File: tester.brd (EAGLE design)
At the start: 56 x 67 mm, 72 parts, among them IC1 ATmega8/88/168, K1 NA 05W K, M1 SP6000C-180, P1 250, P2 10k lin, Q1 BC847CSMD, Q2 BC847CSMD, Q3 BC807-40SMD, Q4 8,000 MHz, Q5 BC847CSMD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

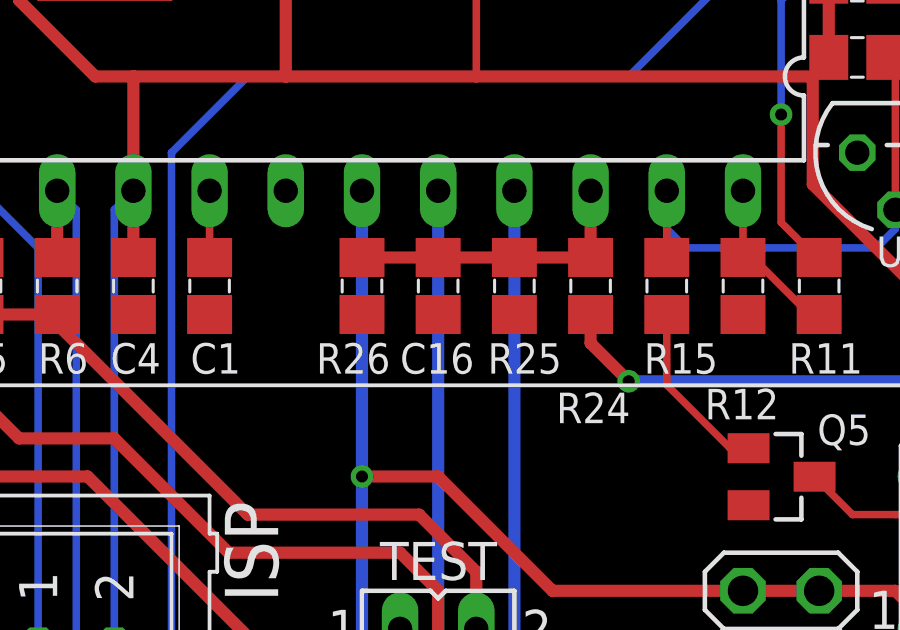
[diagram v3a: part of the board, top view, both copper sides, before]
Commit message: Revert "fix for reichelt"
This reverts commit 00bdf40ca26db270fa33158348546dbcbdb5b146.

Reichelt offers 162K/18K => 1:10-divider
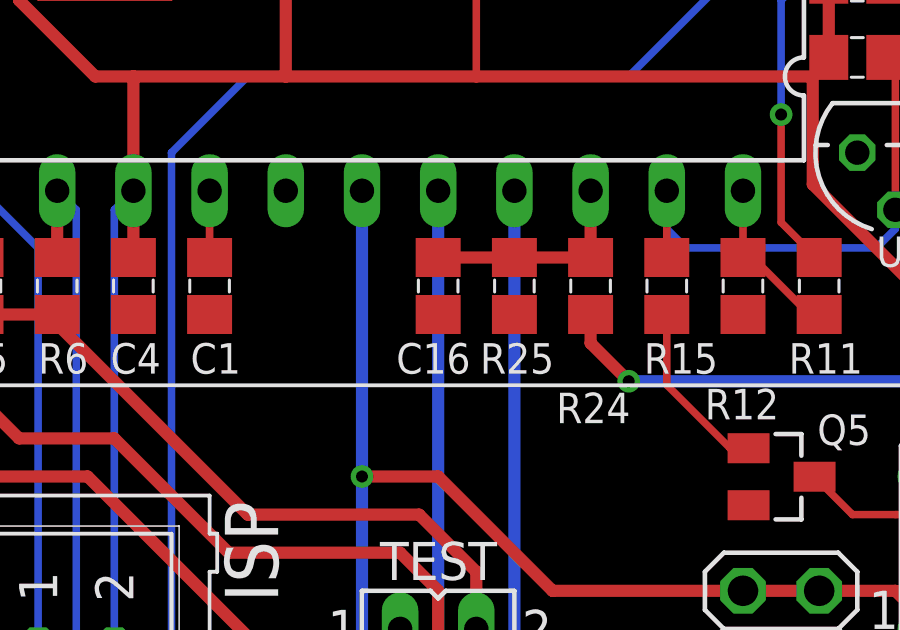
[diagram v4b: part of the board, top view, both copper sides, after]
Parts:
- removed R26: inf, resistor:R0805
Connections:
- net GND: no longer R26.1
- net PC3: no longer R26.2
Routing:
- net PC3: track 10.2 -> 7.45 mm
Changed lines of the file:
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@@
 <variantdefs>
 <variantdef name="nopwm"/>
-<variantdef name="no20k"/>
 </variantdefs>
 <classes>
@@
 <element name="R25" library="resistor" package="R0805" value="20k" x="30.48" y="25.4" smashed="yes" rot="R90">
 <attribute name="TOLERANCE" value="0.1%" x="30.48" y="25.4" size="1.778" layer="27" rot="R90" display="off"/>
-<attribute name="NAME" x="29.591" y="22.479" size="1.016" layer="25"/>
+<attribute name="NAME" x="29.337" y="22.479" size="1.016" layer="25"/>
 <attribute name="VALUE" x="32.512" y="24.511" size="1.27" layer="27" rot="R90"/>
-<variant name="no20k" value="22k"/>
 </element>
 <element name="C16" library="rcl" package="C0805" value="10n" x="27.94" y="25.4" smashed="yes" rot="R270">
-<attribute name="NAME" x="26.67" y="22.479" size="1.016" layer="25"/>
+<attribute name="NAME" x="26.543" y="22.479" size="1.016" layer="25"/>
 <attribute name="VALUE" x="26.035" y="26.035" size="1.27" layer="27" rot="R270"/>
 </element>
@@
 <element name="JP7" library="con-lsta" package="FE02-1" value="TEST2" x="27.94" y="13.97" smashed="yes">
 <attribute name="VALUE" x="25.4" y="11.176" size="1.27" layer="27" ratio="10"/>
-</element>
-<element name="R26" library="resistor" package="R0805" value="inf" x="25.4" y="25.4" smashed="yes" rot="R90">
-<attribute name="TOLERANCE" value="0.1%" x="25.4" y="25.4" size="1.778" layer="27" rot="R90" display="off"/>
-<attribute name="NAME" x="23.876" y="22.479" size="1.016" layer="25"/>
-<attribute name="VALUE" x="27.94" y="24.13" size="1.27" layer="27" rot="R90"/>
-<variant name="no20k" value="220k"/>
 </element>
 </elements>
@@
 <contactref element="Q5" pad="2"/>
 <contactref element="P2" pad="E"/>
-<contactref element="R26" pad="1"/>
 </signal>
 <signal name="N$5">
@@
 <wire x1="28.04" y1="26.25" x2="27.94" y2="26.35" width="0.4064" layer="1"/>
 <wire x1="30.48" y1="26.35" x2="27.94" y2="26.35" width="0.4064" layer="1"/>
-<contactref element="R26" pad="2"/>
-<wire x1="28.04" y1="26.25" x2="28.04" y2="26.35" width="0.4064" layer="1"/>
-<wire x1="28.04" y1="26.35" x2="25.4" y2="26.35" width="0.4064" layer="1"/>
 </signal>
 <signal name="N$24">

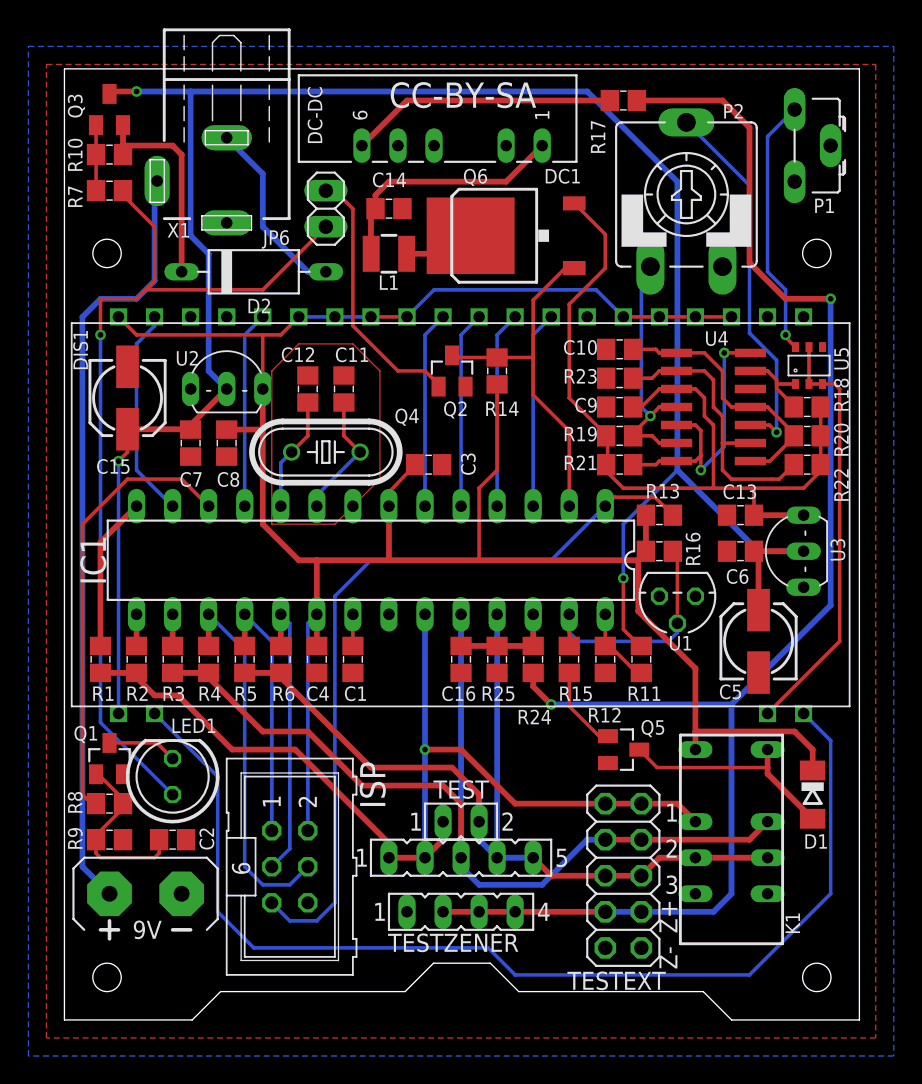
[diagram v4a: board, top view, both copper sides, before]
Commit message: corrected angles
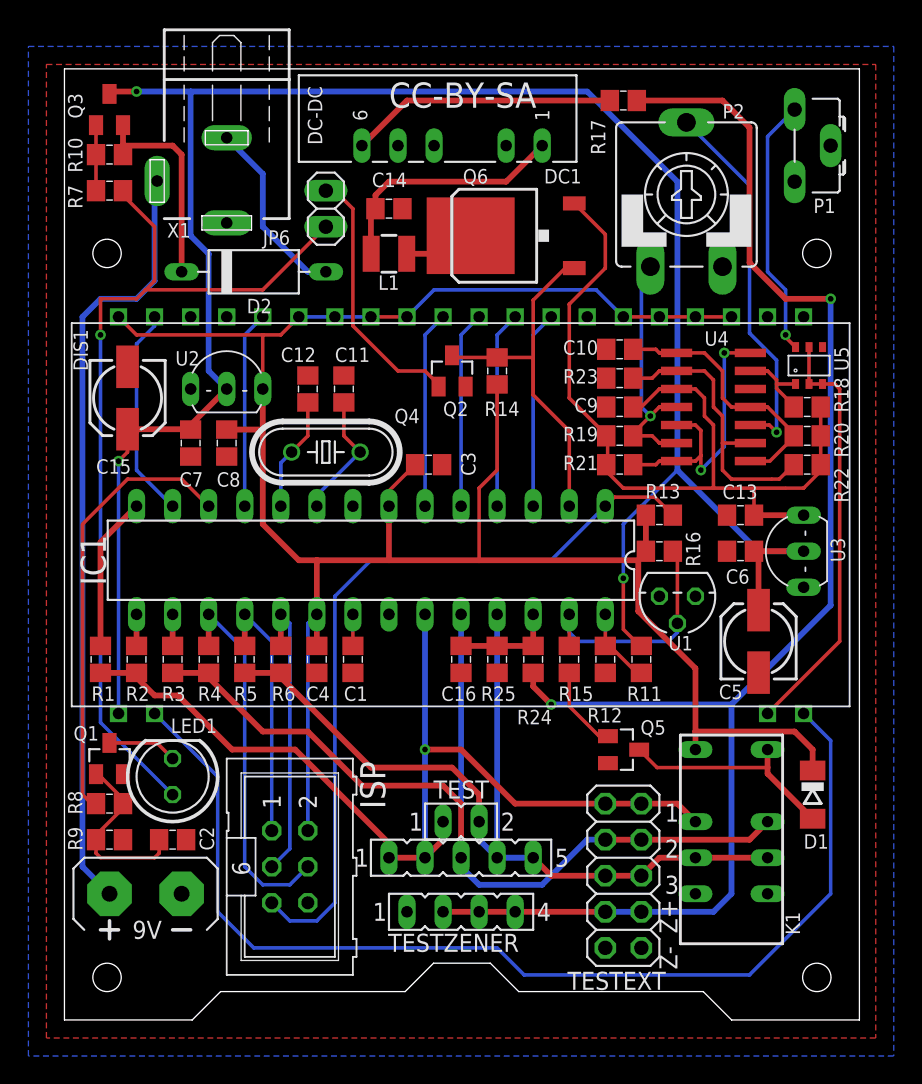
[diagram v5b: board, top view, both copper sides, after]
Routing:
- net N$14: track 34.8 -> 0.00 mm
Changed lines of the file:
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@@
 <rectangle x1="51.07" y1="45.2" x2="52.17" y2="45.3" layer="41"/>
 <rectangle x1="52.67" y1="45.2" x2="53.87" y2="45.3" layer="41"/>
+<wire x1="16.51" y1="47.625" x2="20.32" y2="47.625" width="0.254" layer="41"/>
+<wire x1="20.32" y1="47.625" x2="22.225" y2="45.72" width="0.254" layer="41"/>
+<wire x1="22.225" y1="45.72" x2="22.225" y2="38.1" width="0.254" layer="41"/>
+<wire x1="22.225" y1="38.1" x2="20.955" y2="36.83" width="0.254" layer="41"/>
+<wire x1="19.685" y1="35.56" x2="19.05" y2="34.925" width="0.254" layer="41"/>
+<wire x1="19.05" y1="34.925" x2="14.605" y2="34.925" width="0.254" layer="41"/>
+<wire x1="14.605" y1="34.925" x2="14.605" y2="45.72" width="0.254" layer="41"/>
+<wire x1="14.605" y1="45.72" x2="16.51" y2="47.625" width="0.254" layer="41"/>
 </plain>
 <attributes>
@@
 <wire x1="29.21" y1="37.465" x2="29.21" y2="32.385" width="0.254" layer="1"/>
 <wire x1="22.86" y1="36.195" x2="22.86" y2="37.172" width="0.254" layer="1"/>
-<wire x1="22.86" y1="37.172" x2="24.704" y2="39.116" width="0.254" layer="1"/>
 <wire x1="29.21" y1="32.385" x2="40.425" y2="32.385" width="0.4064" layer="1"/>
 <wire x1="13.97" y1="34.925" x2="13.97" y2="41.59" width="0.4064" layer="1"/>
@@
 <wire x1="40.425" y1="32.385" x2="40.425" y2="32.485" width="0.25" layer="1"/>
 <wire x1="40.425" y1="32.485" x2="40.96" y2="33.02" width="0.25" layer="1"/>
+<wire x1="22.86" y1="37.172" x2="22.86" y2="37.272" width="0.25" layer="1"/>
+<wire x1="22.86" y1="37.272" x2="24.704" y2="39.116" width="0.25" layer="1"/>
 </signal>
 <signal name="PC0">
@@
 <contactref element="DC1" pad="1"/>
 <contactref element="L1" pad="2"/>
-<wire x1="21.61" y1="53.975" x2="21.59" y2="54.095" width="0.4064" layer="1"/>
 <wire x1="21.59" y1="54.095" x2="21.59" y2="57.15" width="0.4064" layer="1"/>
 <wire x1="21.59" y1="57.15" x2="21.91" y2="57.15" width="0.4064" layer="1"/>
@@
 <wire x1="22.86" y1="59.055" x2="31.115" y2="59.055" width="0.4064" layer="1"/>
 <wire x1="31.115" y1="59.055" x2="33.655" y2="61.595" width="0.4064" layer="1"/>
+<wire x1="21.61" y1="53.975" x2="21.59" y2="53.995" width="0.25" layer="1"/>
+<wire x1="21.59" y1="53.995" x2="21.59" y2="54.095" width="0.25" layer="1"/>
 </signal>
 <signal name="N$28">
@@
 <wire x1="10.795" y1="17.145" x2="10.795" y2="7.62" width="0.254" layer="16"/>
 <wire x1="10.795" y1="7.62" x2="13.335" y2="5.08" width="0.254" layer="16"/>
-<wire x1="13.335" y1="5.08" x2="29.845" y2="5.08" width="0.254" layer="16"/>
-<wire x1="29.845" y1="5.08" x2="31.75" y2="3.175" width="0.254" layer="16"/>
-<wire x1="31.75" y1="3.175" x2="48.26" y2="3.175" width="0.254" layer="16"/>
+<wire x1="13.335" y1="5.08" x2="30.48" y2="5.08" width="0.254" layer="16"/>
+<wire x1="30.48" y1="5.08" x2="32.385" y2="3.175" width="0.254" layer="16"/>
+<wire x1="32.385" y1="3.175" x2="48.26" y2="3.175" width="0.254" layer="16"/>
 <wire x1="48.26" y1="3.175" x2="53.975" y2="8.89" width="0.254" layer="16"/>
 <wire x1="53.975" y1="8.89" x2="53.975" y2="19.685" width="0.254" layer="16"/>
@@
 <wire x1="41.749" y1="17.78" x2="40.486" y2="19.043" width="0.25" layer="1"/>
 </signal>
-<signal name="N$14">
-<wire x1="19.685" y1="35.56" x2="19.05" y2="34.925" width="0" layer="1"/>
-<wire x1="19.05" y1="34.925" x2="14.605" y2="34.925" width="0" layer="1"/>
-<wire x1="14.605" y1="34.925" x2="14.605" y2="45.72" width="0" layer="1"/>
-<wire x1="14.605" y1="45.72" x2="16.51" y2="47.625" width="0" layer="1"/>
-<wire x1="16.51" y1="47.625" x2="20.32" y2="47.625" width="0" layer="1"/>
-<wire x1="20.32" y1="47.625" x2="22.225" y2="45.72" width="0" layer="1"/>
-<wire x1="22.225" y1="45.72" x2="22.225" y2="38.1" width="0" layer="1"/>
-<wire x1="22.225" y1="38.1" x2="20.955" y2="36.83" width="0" layer="1"/>
-</signal>
 </signals>
+<errors>
+</errors>
 </board>
 </drawing>

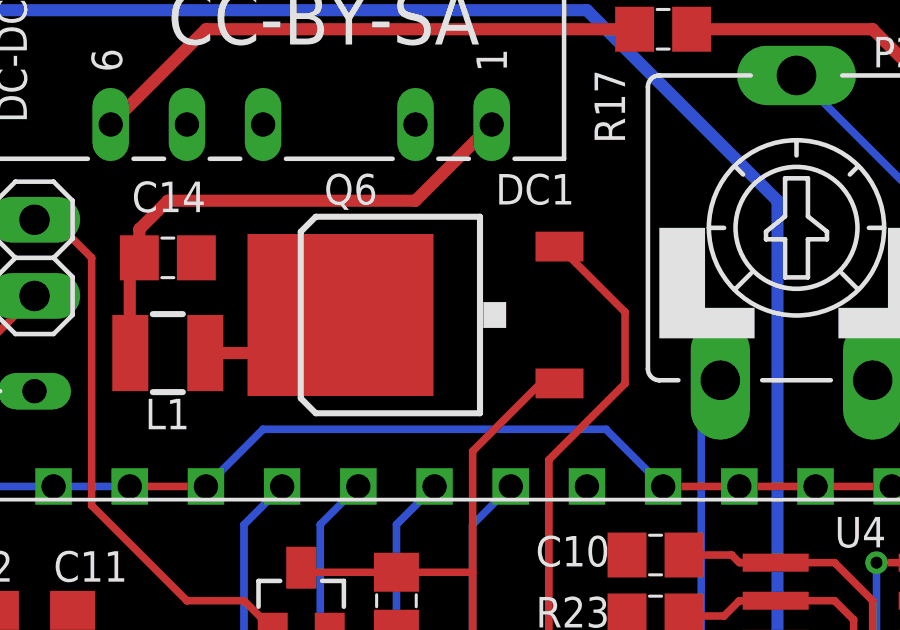
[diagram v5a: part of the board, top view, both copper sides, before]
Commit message: IRLML 6402 for Q6
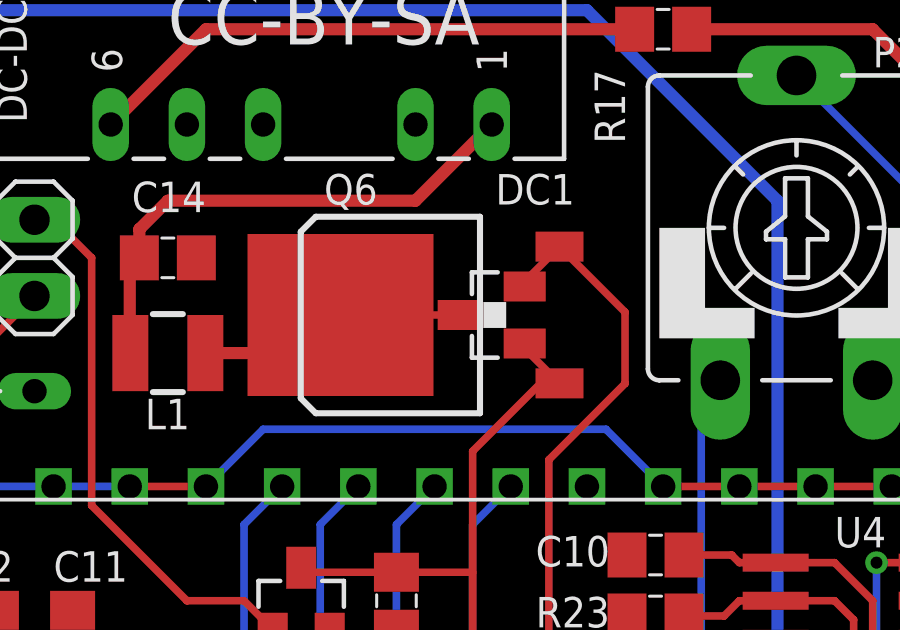
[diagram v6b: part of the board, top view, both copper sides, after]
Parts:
- added Q6/B: IRLML6402, mosfet:MICRO3
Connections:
- net +5V/2: now also Q6/B.2
- net N$24: now also Q6/B.3
- net PD0: now also Q6/B.1
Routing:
- net N$24: track 5.03 -> 8.97 mm
- net +5V/2: track 60.6 -> 62.4 mm
- net PD0: track 28.3 -> 30.1 mm
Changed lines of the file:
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@@
 <attribute name="VALUE" x="25.4" y="11.176" size="1.27" layer="27" ratio="10"/>
+</element>
+<element name="Q6/B" library="mosfet" package="MICRO3" value="IRLML6402" x="33.655" y="55.245" smashed="yes" rot="R90">
+<attribute name="VALUE" x="36.83" y="53.34" size="1.27" layer="27" rot="R90"/>
 </element>
 </elements>
@@
 <wire x1="28.615" y1="55.245" x2="27.345" y2="53.975" width="0.4064" layer="1"/>
 <wire x1="27.345" y1="53.975" x2="24.11" y2="53.975" width="0.4064" layer="1"/>
+<contactref element="Q6/B" pad="3"/>
+<wire x1="28.615" y1="55.245" x2="32.555" y2="55.245" width="0.25" layer="1"/>
 </signal>
 <signal name="N$25">
@@
 <wire x1="38.266" y1="38.569" x2="38.266" y2="39.016" width="0.25" layer="1"/>
 <wire x1="38.266" y1="39.016" x2="38.166" y2="39.116" width="0.25" layer="1"/>
+<contactref element="Q6/B" pad="2"/>
+<wire x1="34.755" y1="56.195" x2="34.755" y2="56.365" width="0.25" layer="1"/>
+<wire x1="34.755" y1="56.365" x2="35.915" y2="57.525" width="0.25" layer="1"/>
 </signal>
 <signal name="V+">
@@
 <wire x1="30.48" y1="46.67" x2="27.305" y2="46.67" width="0.25" layer="1"/>
 <wire x1="27.305" y1="46.67" x2="27.305" y2="46.82" width="0.25" layer="1"/>
+<contactref element="Q6/B" pad="1"/>
+<wire x1="34.755" y1="54.295" x2="34.755" y2="54.125" width="0.25" layer="1"/>
+<wire x1="34.755" y1="54.125" x2="35.915" y2="52.965" width="0.25" layer="1"/>
 </signal>
 <signal name="PD4">
@@
 </signal>
 </signals>
-<errors>
-</errors>
 </board>
 </drawing>

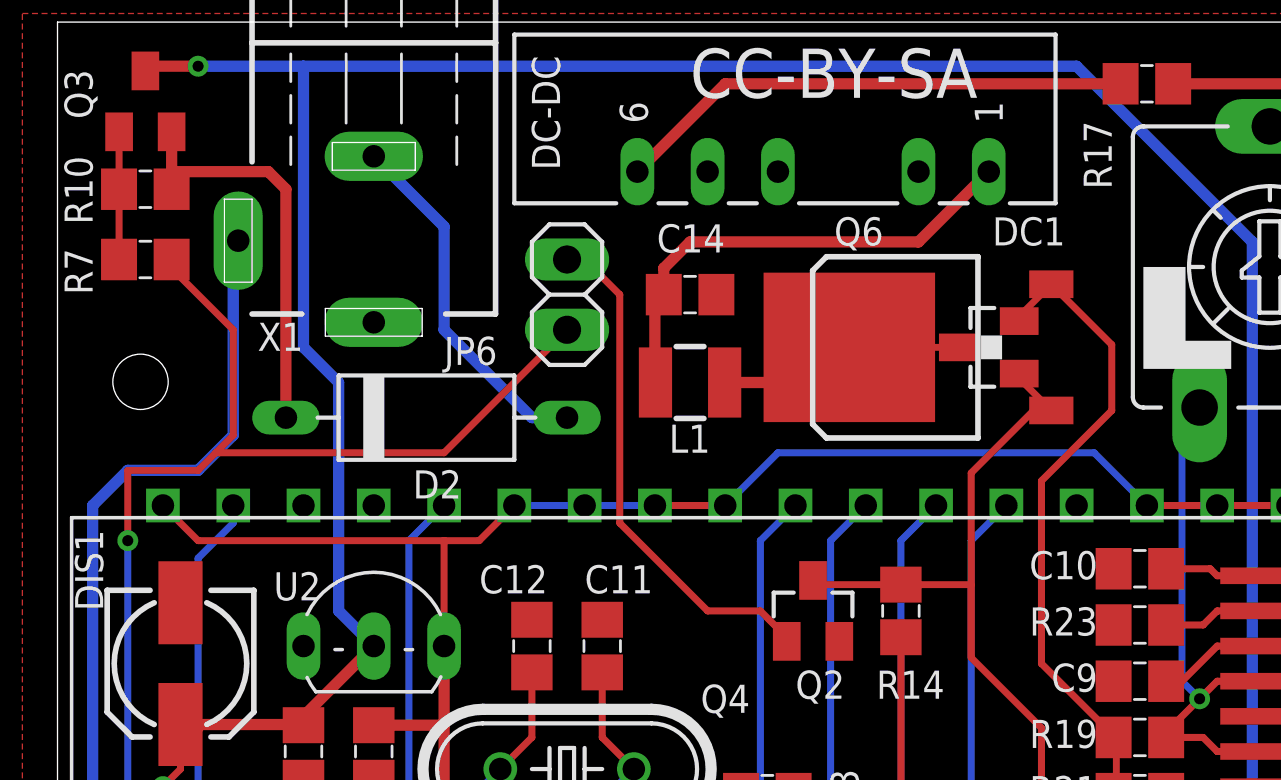
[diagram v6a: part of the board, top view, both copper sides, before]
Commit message: change q6, s1
remove q6 option for irfr9024
tactile switch s1 instead of pin header
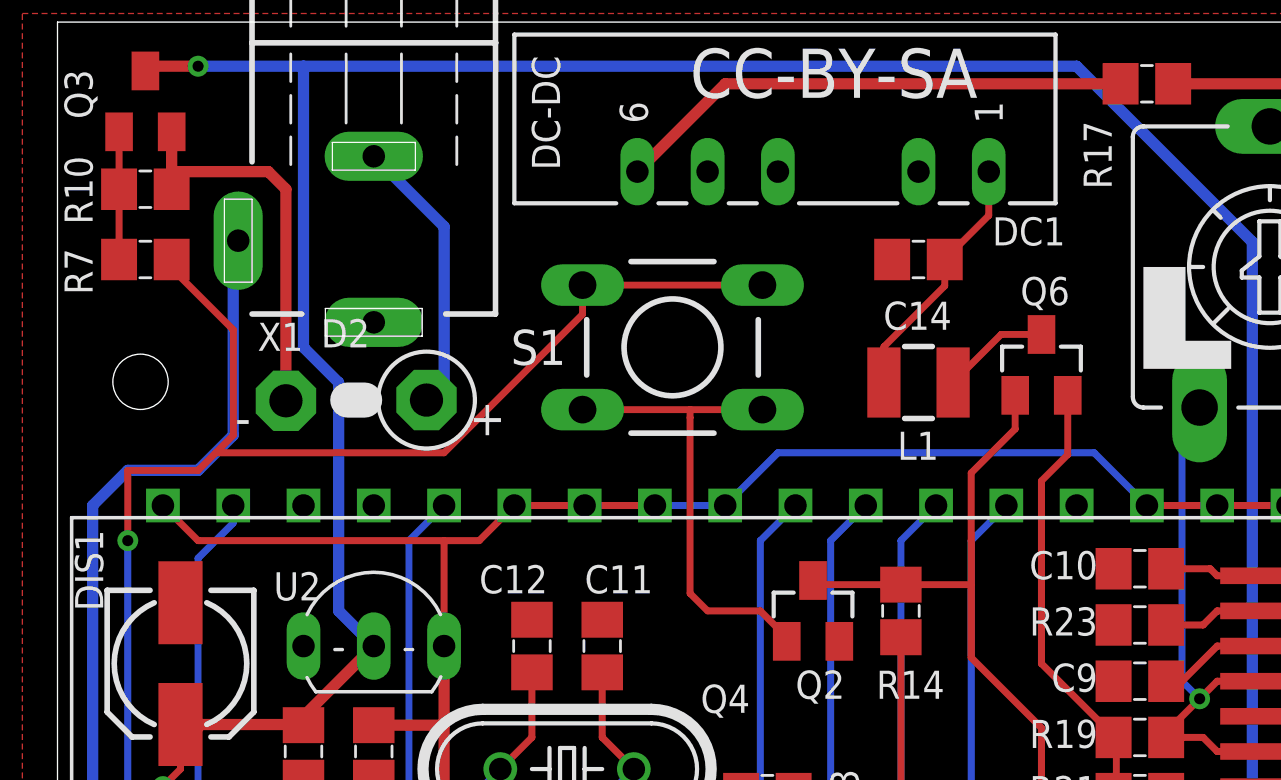
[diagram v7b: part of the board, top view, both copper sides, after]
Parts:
- removed JP6: POWERSW, pinhead:1X02
- removed Q6/B: IRLML6402, mosfet:MICRO3
- added S1: DTS-6, switch-tact:DTS-6
- D2: device markus:DIODE-3-10 -> markus:DIODE-3-5A-V
- Q6: value IRFR9024 -> IRLML6402; device transistor-power:D-PAK_TO252AA -> mosfet:MICRO3
- moved C14 8.35 mm to (31.1, 58.4), turned to 180 degrees
- moved L1 8.25 mm to (31.1, 54.0)
- moved Q6 4.49 mm to (35.6, 54.6), turned to 0 degrees
- moved D2 2.62 mm to (10.8, 53.3), turned to 180 degrees
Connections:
- net +5V/2: now also Q6.2; no longer Q6.3, Q6/B.2
- net N$21: now also S1.1, S1.2; no longer JP6.2
- net N$24: now also Q6.3; no longer Q6.4, Q6/B.3
- net N$3: now also S1.3, S1.4; no longer JP6.1
- net PD0: no longer Q6/B.1
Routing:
- net N$25: track 17.6 -> 9.19 mm
- net N$21: track 63.3 -> 71.6 mm
- net +5V/2: track 62.4 -> 55.0 mm
- net N$24: track 8.97 -> 3.91 mm
- net N$11: track 13.1 -> 10.1 mm
- net PD0: track 30.1 -> 27.9 mm
- net N$3: track 18.6 -> 17.4 mm
- net N$5: track 15.0 -> 14.4 mm
